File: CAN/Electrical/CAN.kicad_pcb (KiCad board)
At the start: 2 copper layers, 26 x 30 mm, 21 parts, among them J3 Screw_Terminal_01x04, P1 USB_C_Plug_USB2.0, Q1 BSS214NW, Q2 BSS214NW, U1 AP2112K-3.3, U2 SN65HVD230, U5 ESP32-C3-MINI-1

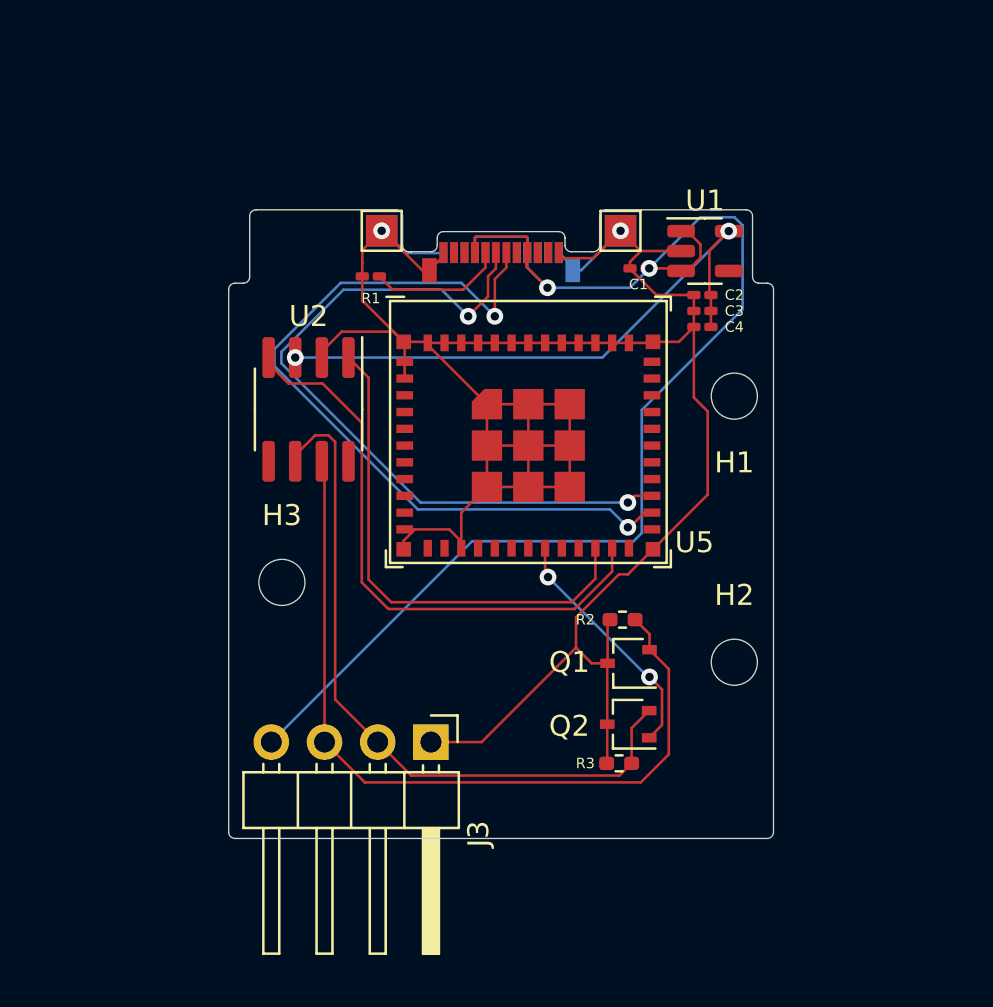
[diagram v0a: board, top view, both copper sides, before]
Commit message: Replaced Footprints
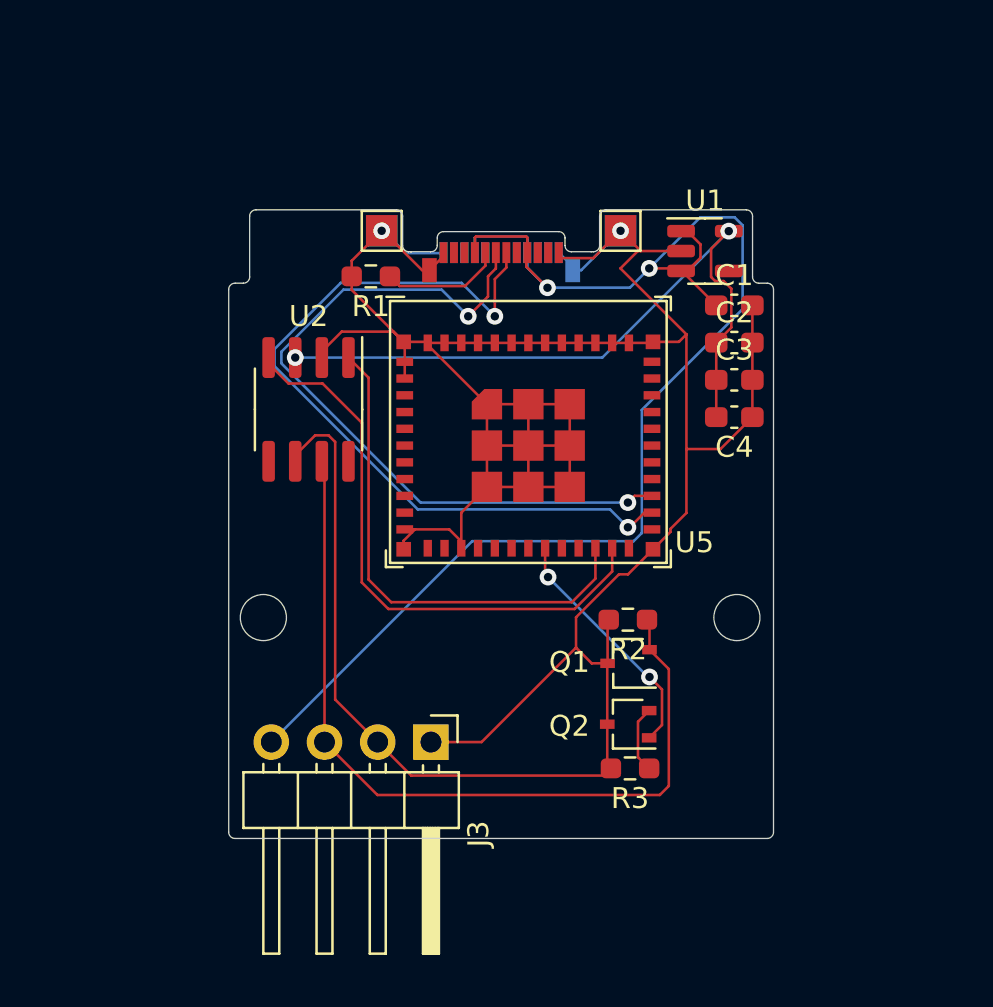
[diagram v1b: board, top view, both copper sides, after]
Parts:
- removed H3: MountingHole, MountingHole:MountingHole_2.2mm_M2
- C1, C2, C3, C4: footprint Capacitor_SMD:C_0201_0603Metric_Pad0.64x0.40mm_HandSolder -> Capacitor_SMD:C_0603_1608Metric_Pad1.08x0.95mm_HandSolder
- R1: footprint Resistor_SMD:R_0201_0603Metric_Pad0.64x0.40mm_HandSolder -> Resistor_SMD:R_0603_1608Metric_Pad0.98x0.95mm_HandSolder
- R2, R3: footprint Resistor_SMD:R_0402_1005Metric_Pad0.72x0.64mm_HandSolder -> Resistor_SMD:R_0603_1608Metric_Pad0.98x0.95mm_HandSolder
- moved H1 24.8 mm to (63.9, 105.8)
- moved C1 4.90 mm to (86.4, 90.9), turned to 0 degrees
- moved C4 4.57 mm to (86.4, 96.3)
- moved C3 3.62 mm to (86.4, 94.5), turned to 0 degrees
- moved C2 2.74 mm to (86.4, 92.7), turned to 0 degrees
- moved H2 2.14 mm to (86.5, 105.8)
- moved R3 0.57 mm to (81.4, 113.0)
- moved R2 0.25 mm to (81.3, 105.9)
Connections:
- C4 pad 1: +3V3 -> GND
- C4 pad 2: GND -> +3V3
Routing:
- net GND: track 123.8 -> 131.9 mm
- net +3V3: track 28.2 -> 33.4 mm
- net VBUS: track 66.3 -> 68.7 mm
- net CAN_H: track 38.3 -> 39.5 mm
- net Net-(P1-CC): track 6.48 -> 5.77 mm

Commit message: Fixed S
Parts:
- renumbered J3 to J1
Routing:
- net /TERM: track 11.7 -> 14.3 mm
- net CAN_H: track 39.5 -> 40.7 mm
- net VBUS: track 68.7 -> 69.7 mm
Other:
- board text added: "CAN Transceiver"
- board text added: "Termination Resistor"

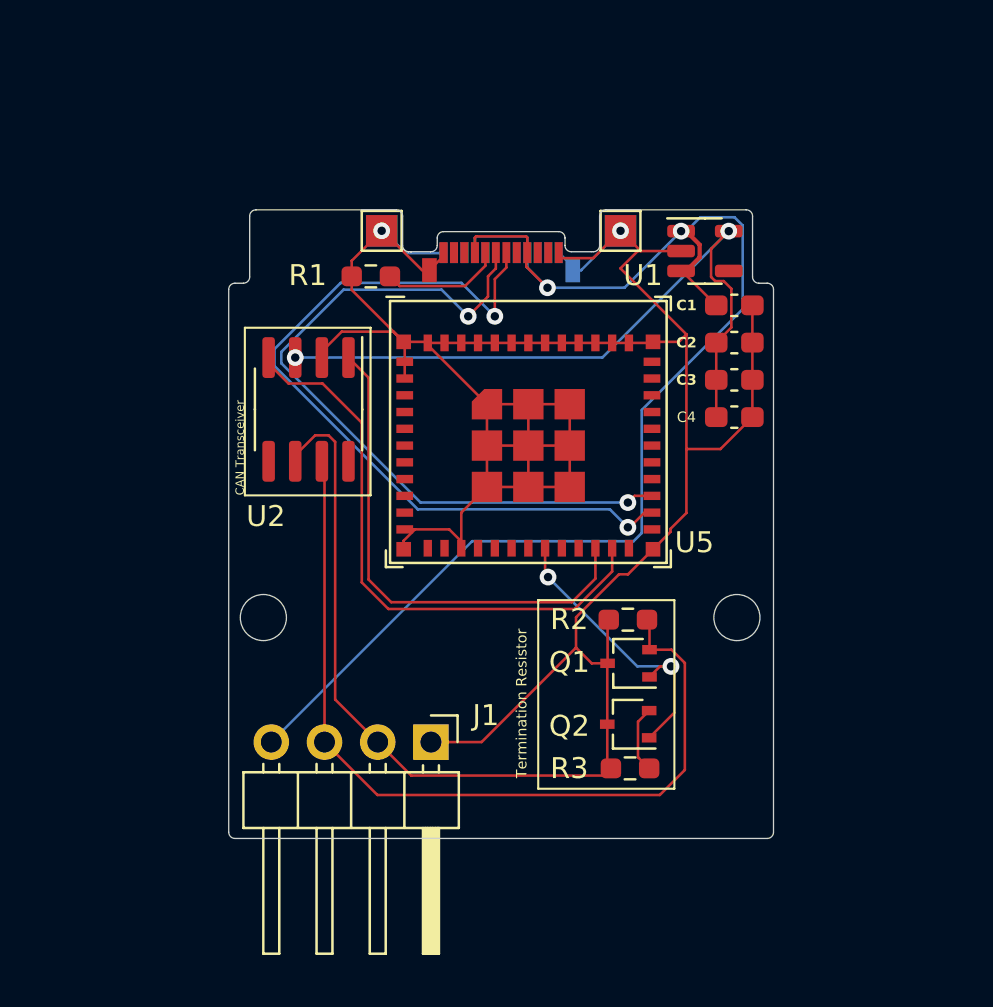
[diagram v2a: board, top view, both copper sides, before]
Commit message: Replaced Screw terminal with pin socket
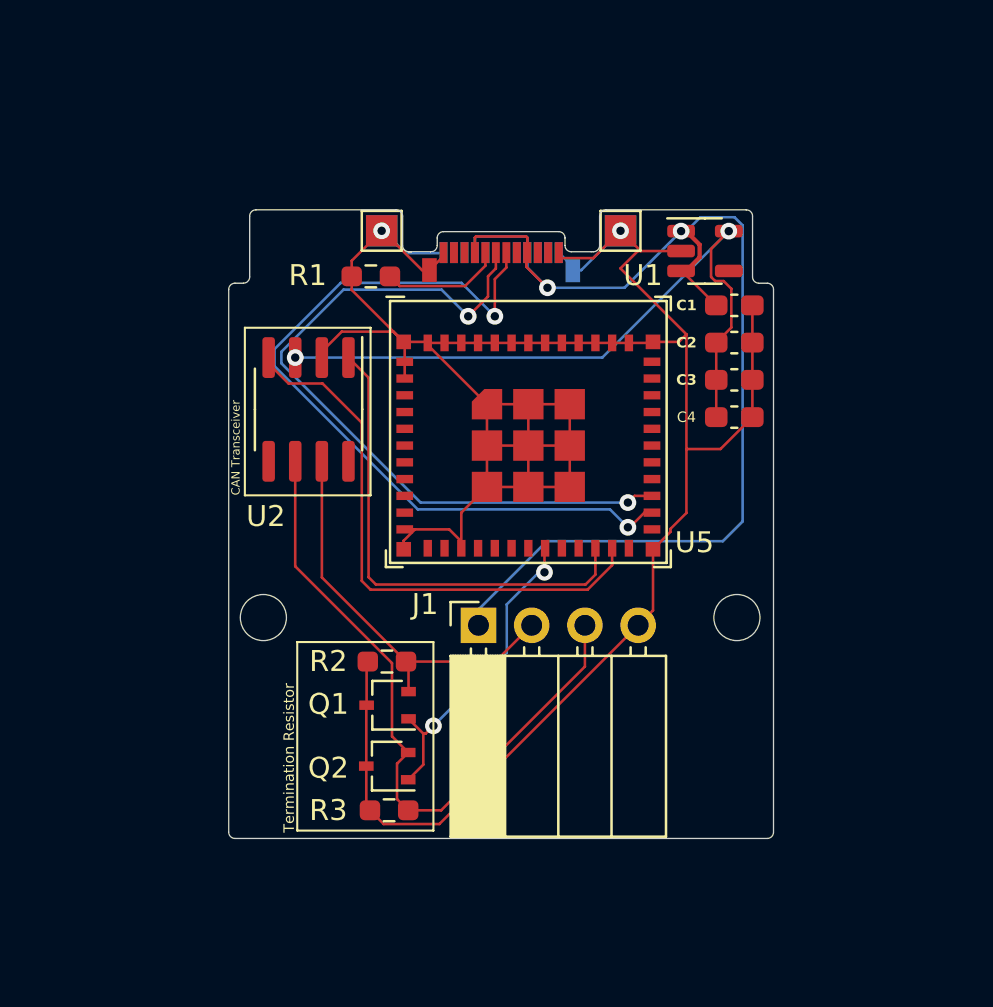
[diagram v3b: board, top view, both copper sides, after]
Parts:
- J1: value Screw_Terminal_01x04 -> Conn_01x04; footprint Connector_PinHeader_2.54mm:PinHeader_1x04_P2.54mm_Horizontal -> Connector_PinSocket_2.54mm:PinSocket_1x04_P2.54mm_Horizontal
- moved Q1 11.7 mm to (69.8, 110.0)
- moved Q2 11.7 mm to (69.8, 112.9)
- moved R2 11.7 mm to (69.8, 107.9)
- moved R3 11.7 mm to (69.9, 115.0)
- moved J1 6.02 mm to (74.2, 106.2), turned to 90 degrees
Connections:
- J1 pad 1: GND -> VBUS
- J1 pad 2: CAN_L -> CAN_H
- J1 pad 3: CAN_H -> CAN_L
- J1 pad 4: VBUS -> GND
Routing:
- net CAN_H: track 40.7 -> 19.4 mm
- net VBUS: track 69.7 -> 60.4 mm
- net GND: track 131.9 -> 135.5 mm
- net /CAN_RX: track 27.8 -> 26.9 mm
- net /CAN_TX: track 24.2 -> 23.3 mm
- net CAN_L: track 33.3 -> 32.6 mm
- net /TERM: track 14.3 -> 15.0 mm

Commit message: Updated PCB
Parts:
- added TP5: TestPoint, TestPoint:TestPoint_Pad_1.5x1.5mm, F.Cu at (64.8, 87.9)
- added TP6: TestPoint, TestPoint:TestPoint_Pad_1.5x1.5mm, F.Cu at (64.8, 90.6)
- added TP7: TestPoint, TestPoint:TestPoint_Pad_1.5x1.5mm, B.Cu at (64.8, 87.9)
- added TP8: TestPoint, TestPoint:TestPoint_Pad_1.5x1.5mm, B.Cu at (64.8, 90.6)
- C1, C2, C3, C4: footprint Capacitor_SMD:C_0603_1608Metric_Pad1.08x0.95mm_HandSolder -> Capacitor_SMD:C_0805_2012Metric_Pad1.18x1.45mm_HandSolder
- R1: footprint Resistor_SMD:R_0603_1608Metric_Pad0.98x0.95mm_HandSolder -> Resistor_SMD:R_0805_2012Metric_Pad1.20x1.40mm_HandSolder
- moved H1 22.6 mm to (86.5, 105.8)
- moved H2 22.6 mm to (63.9, 105.8)
- moved C4 4.83 mm to (86.2, 101.1)
- moved C3 3.30 mm to (86.2, 97.8)
- moved C2 1.91 mm to (86.2, 94.6)
- moved R1 1.83 mm to (67.2, 89.4), turned to -90 degrees
- moved C1 0.52 mm to (86.2, 91.4)
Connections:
- C2 pad 1: +3V3 -> +3.3V
- C3 pad 1: +3V3 -> +3.3V
- C4 pad 2: +3V3 -> +3.3V
- U1 pad 5: +3V3 -> +3.3V
- U2 pad 3: +3V3 -> +3.3V
- U5 pad 8: unconnected-(U5-EN/CHIP_PU-Pad8) -> +3.3V
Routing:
- net +3.3V: track 0.00 -> 51.2 mm, vias 0 -> 4
- net +3V3: track 33.4 -> 0.00 mm, vias 2 -> 0
- net VBUS: track 60.4 -> 71.2 mm, vias 2 -> 3
- net Net-(P1-CC): track 5.77 -> 9.81 mm, vias 0 -> 2
- net GND: track 135.5 -> 139.4 mm
- net /D+: track 35.4 -> 34.6 mm
- net /D-: track 38.1 -> 37.4 mm
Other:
- board text removed: "CAN Transceiver"
- board text removed: "Termination Resistor"

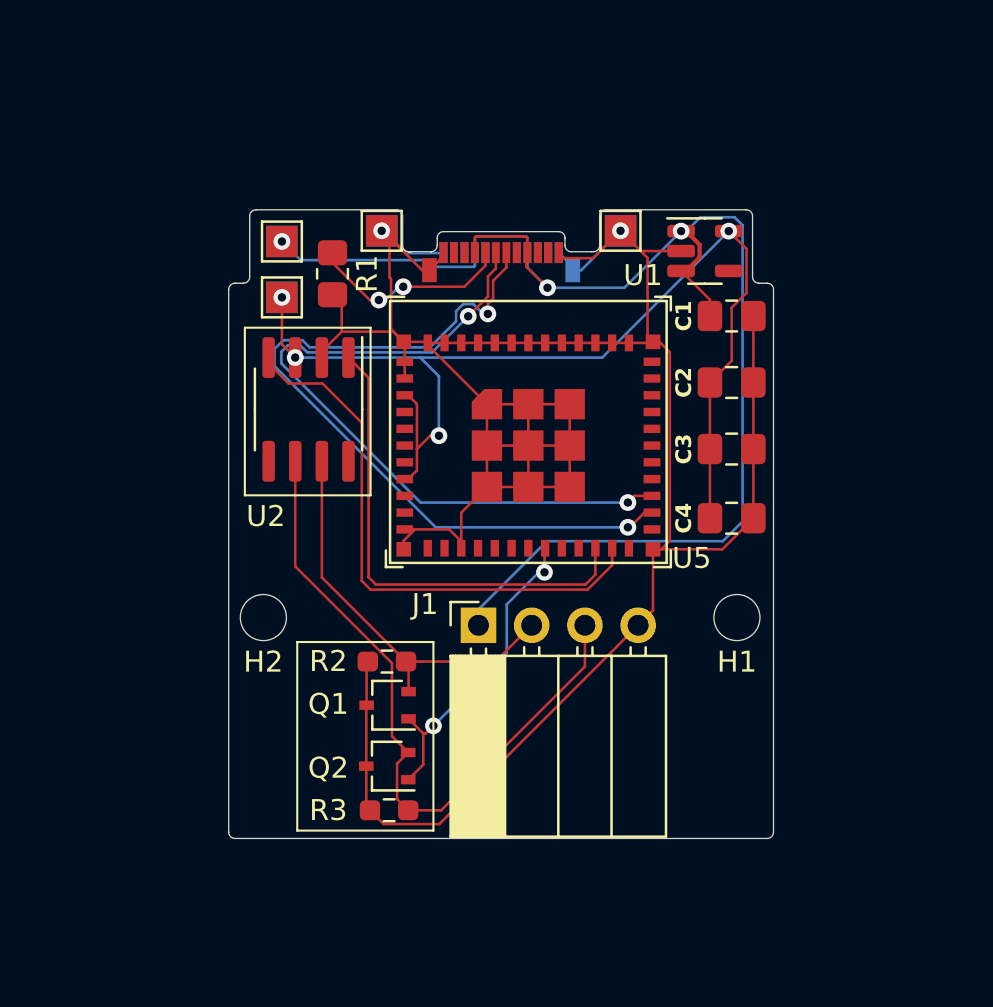
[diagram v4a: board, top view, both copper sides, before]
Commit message: Updated Board
Added Ground Plane and power plane
Updated PCB from Schematic
Changed to 4 layers
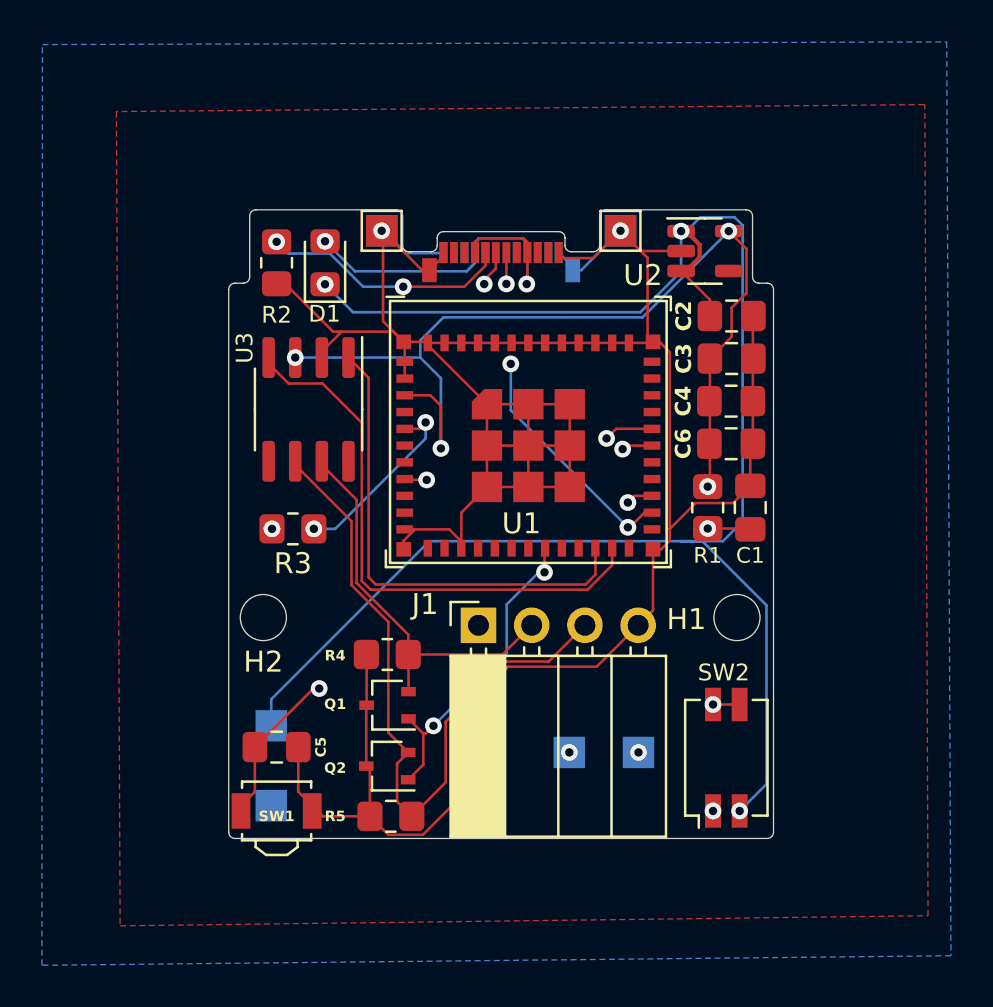
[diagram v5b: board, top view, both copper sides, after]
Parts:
- added C1: 1uF, Capacitor_SMD:C_0805_2012Metric_Pad1.18x1.45mm_HandSolder, F.Cu at (87.1, 100.6)
- added C5: 0.1uF, Capacitor_SMD:C_0805_2012Metric_Pad1.18x1.45mm_HandSolder, F.Cu at (64.5, 112.0)
- added D1: D, Diode_SMD:D_0805_2012Metric_Pad1.15x1.40mm_HandSolder, F.Cu at (66.8, 88.9)
- added R1: 10k, Resistor_SMD:R_0805_2012Metric_Pad1.20x1.40mm_HandSolder, F.Cu at (85.1, 100.6)
- added R3: 10k, Resistor_SMD:R_0805_2012Metric_Pad1.20x1.40mm_HandSolder, F.Cu at (65.3, 101.6)
- added SW1: SW_Push, Button_Switch_SMD:SW_SPST_B3U-3000P, F.Cu at (64.5, 115.1)
- added SW2: SW_DIP_x02, Button_Switch_SMD:SW_DIP_SPSTx02_Slide_Copal_CHS-02A_W5.08mm_P1.27mm_JPin, F.Cu at (86.0, 112.5)
- C4: renamed from C3; value 22uF -> 10uF
- C6: renamed from C4; value 100nF -> 0.1uF
- R4: renamed from R2; footprint Resistor_SMD:R_0603_1608Metric_Pad0.98x0.95mm_HandSolder -> Resistor_SMD:R_0805_2012Metric_Pad1.20x1.40mm_HandSolder
- R5: renamed from R3; footprint Resistor_SMD:R_0603_1608Metric_Pad0.98x0.95mm_HandSolder -> Resistor_SMD:R_0805_2012Metric_Pad1.20x1.40mm_HandSolder
- TP5, TP6: moved to B.Cu
- TP7: value TestPoint -> TX
- TP8: value TestPoint -> RX
- moved TP7 28.0 mm to (78.5, 112.3)
- moved TP8 27.6 mm to (81.8, 112.3)
- moved TP6 24.3 mm to (64.3, 114.8), turned to 180 degrees
- moved TP5 23.1 mm to (64.3, 111.0), turned to 180 degrees
- moved C6 3.56 mm to (86.2, 97.5)
- moved R2 2.72 mm to (64.5, 88.9)
- moved C4 2.29 mm to (86.2, 95.5)
- moved C3 1.14 mm to (86.2, 93.5)
- moved R4 0.34 mm to (69.8, 107.6)
- moved R5 0.30 mm to (70.0, 115.3)
- renumbered C1 to C2, C2 to C3, R1 to R2, TP3 to TP2, TP2 to TP3, U5 to U1, U1 to U2, U2 to U3
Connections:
- J1 pad 1: VBUS -> Net-(J1-Pin_1)
- P1 pad A4: VBUS -> Net-(D1-A)
- P1 pad A9: VBUS -> Net-(D1-A)
- P1 pad B4: VBUS -> Net-(D1-A)
- P1 pad B9: VBUS -> Net-(D1-A)
- TP7 pad 1: VBUS -> /TXD
- TP8 pad 1: +3.3V -> /RXD
- U1 pad 5: unconnected-(U5-GPIO2/ADC1_CH2-Pad5) -> Net-(U1-GPIO2/ADC1_CH2)
- U1 pad 8: +3.3V -> /EN
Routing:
- net /EN: track 0.00 -> 37.5 mm, vias 0 -> 3
- net +3.3V: track 51.2 -> 71.7 mm, vias 4 -> 6
- net /D-: track 37.4 -> 17.6 mm, vias 2 -> 3
- net Net-(D1-A): track 0.00 -> 18.7 mm, vias 0 -> 2
- net VBUS: track 71.2 -> 89.3 mm
- net /TXD: track 0.00 -> 18.1 mm, vias 0 -> 2
- net /D+: track 34.6 -> 17.9 mm
- net /RXD: track 0.00 -> 16.5 mm, vias 0 -> 2
- net Net-(J1-Pin_1): track 0.00 -> 14.0 mm, vias 0 -> 1
- net GND: track 139.4 -> 148.4 mm
- net Net-(U1-GPIO2/ADC1_CH2): track 0.00 -> 9.01 mm, vias 0 -> 2
- net Net-(P1-CC): track 9.81 -> 11.9 mm
- net CAN_L: track 32.6 -> 33.4 mm
- added copper zone on B.Cu, net +3.3V
- added copper zone on F.Cu, net GND
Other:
- copper layers 2 -> 4
